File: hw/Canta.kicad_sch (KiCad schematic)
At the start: 49 parts, among them J1 USB_C_Receptacle_PowerOnly_6P, J101 Conn_01x01, J102 Conn_01x01, J103 Conn_01x01, J104 Conn_01x01, J105 Conn_01x01, J106 Conn_01x01, J107 Conn_01x01, J108 Conn_01x01, J109 Conn_01x01, J110 Conn_01x01, J111 Conn_01x01, J112 Conn_01x01, J2 Conn_01x03, U1 PY32F003F18U6, U2 TM8211, U3 FM8002A, Y1 32MHz 12pF

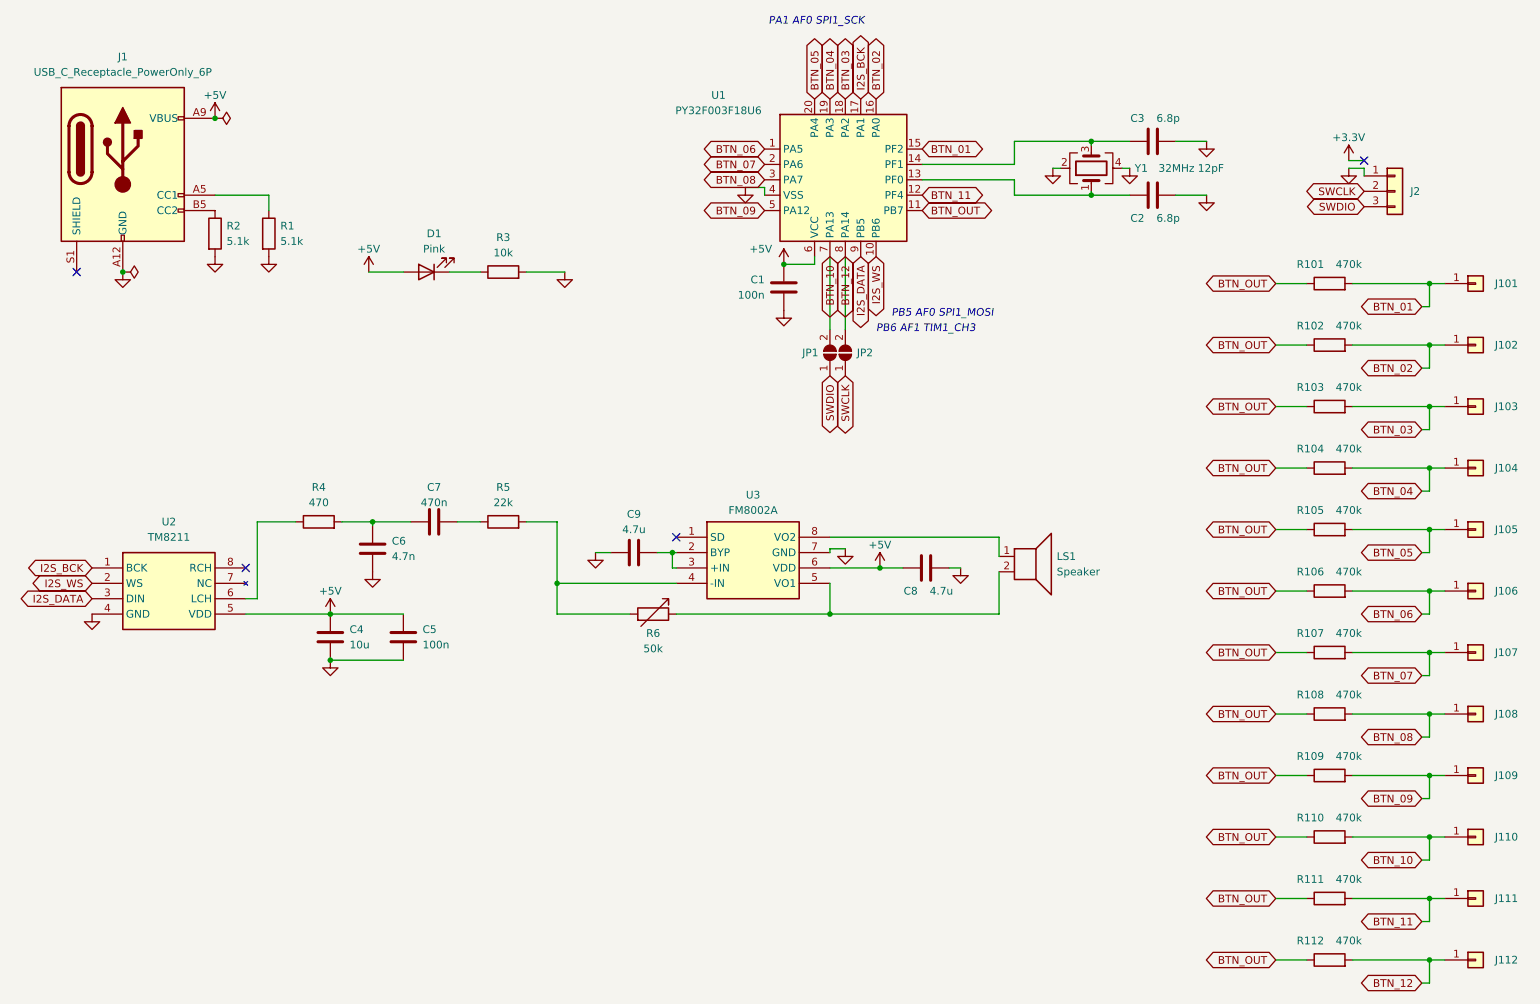
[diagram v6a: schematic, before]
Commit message: Update component values with actual assembly
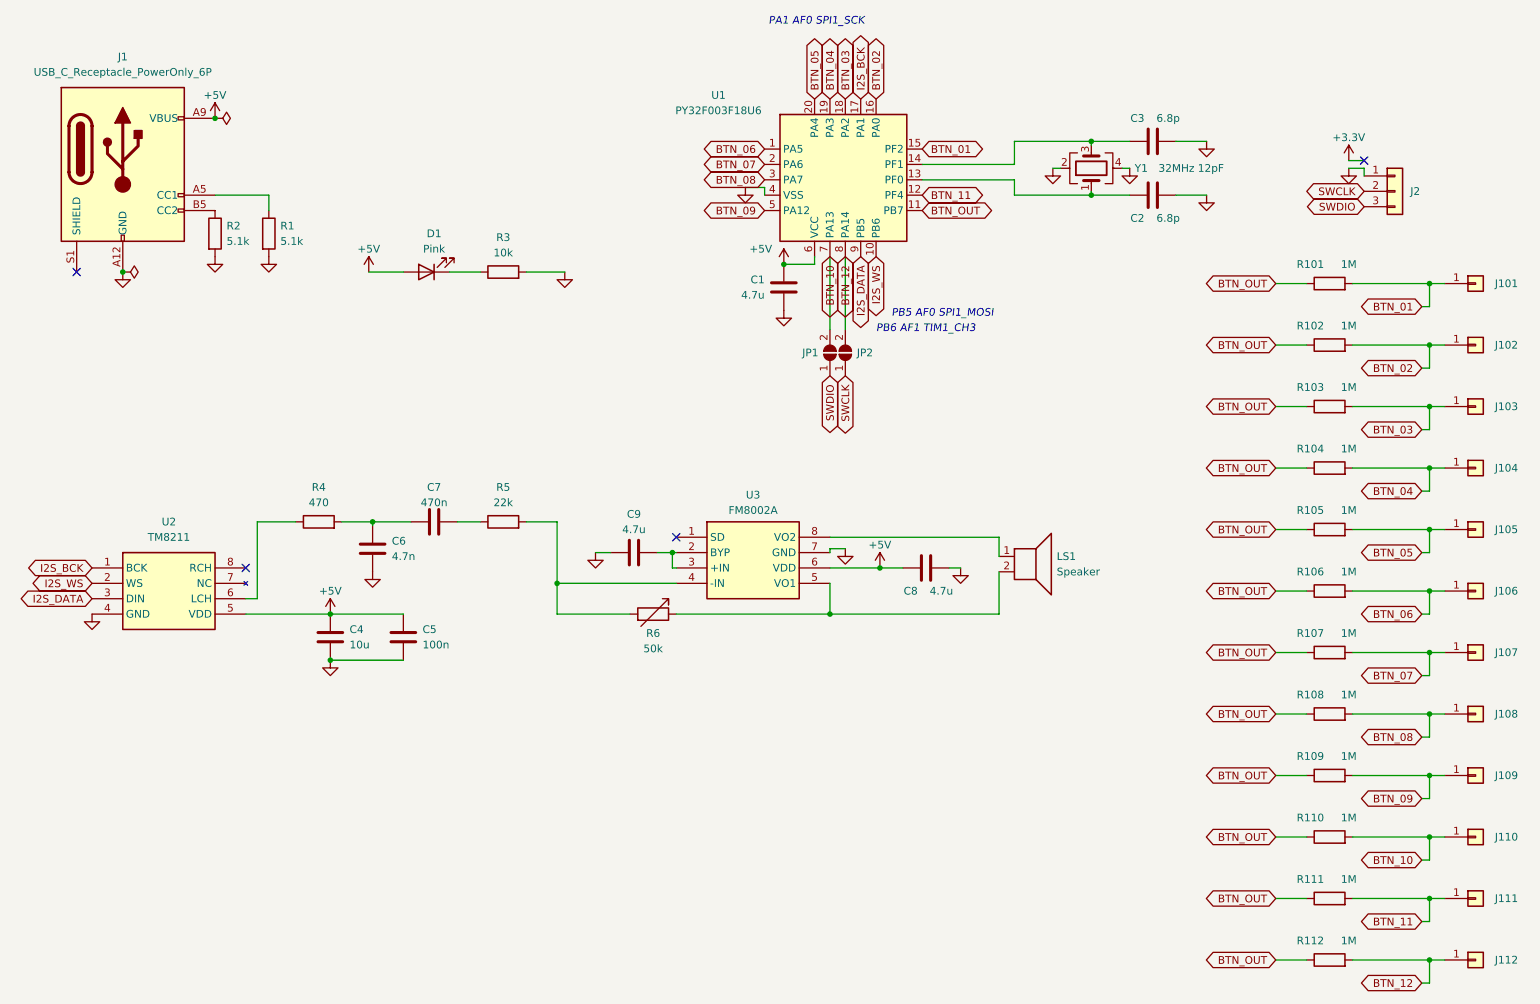
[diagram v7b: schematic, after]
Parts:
- C1: value 100n -> 4.7u
- R101, R102, R103, R104, R105, R106, R107, R108, R109, R110, R111, R112: value 470k -> 1M
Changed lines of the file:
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@@
       (effects (font (size 1.27 1.27)))
     )
-    (property "Value" "470k" (at 245.11 170.18 90)
+    (property "Value" "1M" (at 245.11 170.18 90)
       (effects (font (size 1.27 1.27)))
     )
@@
       (effects (font (size 1.27 1.27)))
     )
-    (property "Value" "470k" (at 245.11 58.42 90)
+    (property "Value" "1M" (at 245.11 58.42 90)
       (effects (font (size 1.27 1.27)))
     )
@@
       (effects (font (size 1.27 1.27)))
     )
-    (property "Value" "470k" (at 245.11 68.58 90)
+    (property "Value" "1M" (at 245.11 68.58 90)
       (effects (font (size 1.27 1.27)))
     )
@@
       (effects (font (size 1.27 1.27)))
     )
-    (property "Value" "470k" (at 245.11 160.02 90)
+    (property "Value" "1M" (at 245.11 160.02 90)
       (effects (font (size 1.27 1.27)))
     )
@@
       (effects (font (size 1.27 1.27)))
     )
-    (property "Value" "470k" (at 245.11 78.74 90)
+    (property "Value" "1M" (at 245.11 78.74 90)
       (effects (font (size 1.27 1.27)))
     )
@@
       (effects (font (size 1.27 1.27)))
     )
-    (property "Value" "470k" (at 245.11 99.06 90)
+    (property "Value" "1M" (at 245.11 99.06 90)
       (effects (font (size 1.27 1.27)))
     )
@@
       (effects (font (size 1.27 1.27)))
     )
-    (property "Value" "470k" (at 245.11 129.54 90)
+    (property "Value" "1M" (at 245.11 129.54 90)
       (effects (font (size 1.27 1.27)))
     )
@@
       (effects (font (size 1.27 1.27)))
     )
-    (property "Value" "470k" (at 245.11 109.22 90)
+    (property "Value" "1M" (at 245.11 109.22 90)
       (effects (font (size 1.27 1.27)))
     )
@@
       (effects (font (size 1.27 1.27)))
     )
-    (property "Value" "470k" (at 245.11 88.9 90)
+    (property "Value" "1M" (at 245.11 88.9 90)
       (effects (font (size 1.27 1.27)))
     )
@@
       (effects (font (size 1.27 1.27)) (justify left))
     )
-    (property "Value" "100n" (at 148.59 63.5 0)
+    (property "Value" "4.7u" (at 148.59 63.5 0)
       (effects (font (size 1.27 1.27)) (justify left))
     )
@@
       (effects (font (size 1.27 1.27)))
     )
-    (property "Value" "470k" (at 245.11 149.86 90)
+    (property "Value" "1M" (at 245.11 149.86 90)
       (effects (font (size 1.27 1.27)))
     )
@@
       (effects (font (size 1.27 1.27)))
     )
-    (property "Value" "470k" (at 245.11 139.7 90)
+    (property "Value" "1M" (at 245.11 139.7 90)
       (effects (font (size 1.27 1.27)))
     )
@@
       (effects (font (size 1.27 1.27)))
     )
-    (property "Value" "470k" (at 245.11 119.38 90)
-      (effects (font (size 1.27 1.27)))
-    )
+    (property "Value" "1M" (at 245.11 119.38 90)
+      (effects (font (size 1.27 1.27)))
+    )

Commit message: Revise hardware design
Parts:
- removed JP1, JP2: SolderJumper_2_Open, Canta_footprints:SolderJumper-2_Open, symbol Jumper:SolderJumper_2_Open
- removed R101, R102, R103, R104, R105, R106, R107, R108, R109, R110, R111, R112: 1M, Resistor_SMD:R_0402_1005Metric, symbol Device:R
- added C10, C11: 1u, Capacitor_SMD:C_0402_1005Metric, symbol Device:C
- added RN1, RN2, RN3: 1M, Resistor_SMD:R_Array_Convex_4x0402, symbol Canta_symbols:R_Network04_Split
- added U4: TLV70245_SOT23-5, Package_TO_SOT_SMD:SOT-23-5, symbol Regulator_Linear:TLV70245_SOT23-5
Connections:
- net SWCLK is gone; now on net BTN_12: J2.2 (Pin_2)
- net SWDIO is gone; now on net BTN_10: J2.3 (Pin_3)
- net +5V: now also C10.1, U4.1 (IN), U4.3 (EN); no longer C1.1, C4.1, C5.1, C8.1, D1.2 (A), U1.6 (VCC), U2.5 (VDD), U3.6 (VDD)
- net BTN_01: now also RN1.7 (R2.2)
- net BTN_02: now also RN1.6 (R3.2)
- net BTN_03: now also RN1.5 (R4.2)
- net BTN_04: now also RN2.8 (R1.2)
- net BTN_05: now also RN2.7 (R2.2)
- net BTN_06: now also RN2.6 (R3.2)
- net BTN_07: now also RN2.5 (R4.2)
- net BTN_08: now also RN3.8 (R1.2)
- net BTN_09: now also RN3.7 (R2.2)
- net BTN_10: now also RN3.6 (R3.2)
- net BTN_11: now also RN1.8 (R1.2)
- net BTN_12: now also RN3.5 (R4.2)
- net BTN_OUT: now also RN1.1 (R1.1), RN1.2 (R2.1), RN1.3 (R3.1), RN1.4 (R4.1), RN2.1 (R1.1), RN2.2 (R2.1), RN2.3 (R3.1), RN2.4 (R4.1), RN3.1 (R1.1), RN3.2 (R2.1), RN3.3 (R3.1), RN3.4 (R4.1)
- net GND: now also C10.2, C11.2, U4.2 (GND)
- new net VDD: C1.1, C11.1, C4.1, C5.1, C8.1, D1.2 (A), U1.6 (VCC), U2.5 (VDD), U3.6 (VDD), U4.5 (OUT)
- no-connect marks 4 -> 3
